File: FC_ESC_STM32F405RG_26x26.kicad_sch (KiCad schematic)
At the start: 233 parts, among them J1 MOTOR, J10 UART4, J12 Conn_02x02_Odd_Even, J13 ALARM, J14 LED_STRIP, J15 RC, J16 MOTOR, J17 MOTOR, J18 MOTOR, J19 MOTOR, J2 Conn_02x04_Odd_Even, J20 USB_A, J21 ESC_PROG, J22 MOTOR, J23 ESC_PROG, J24 ESC_PROG, J25 ESC_PROG, J26 MOTOR, J3 Debugger, J4 MOTOR, J5 RSSI, J6 I2C2_UART3, J7 SD CARD, J8 UART1, J9 UART6, Q1 SIZ200, Q10 SIZ200, Q11 SIZ200, Q12 SIZ200, Q2 SIZ200, Q3 SIZ200, Q4 SIZ200, Q5 SIZ200, Q6 SIZ200, Q7 SIZ200, Q8 SIZ200, Q9 SIZ200, U1 EFM8BB21, U10 FD6288Q, U11 outline, U12 MPU-6000, U13 BMP280, U15 STM32F405RGTx, U16 TPS54331D, U2 EFM8BB21, U3 TPS54560BDDA, U4 FD6288Q, U5 FD6288Q, U6 AT7456, U7 EFM8BB21, U8 EFM8BB21, U9 FD6288Q, Y1 8MHz, Y2 8Mhz

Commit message: update placement
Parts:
- removed J1, J22, J26, J4: MOTOR, Proj_footprint:MountingPad_1x3, symbol Connector_Generic:Conn_01x03
- removed J10: UART4, Proj_footprint:MoutingPad_1x4, symbol Connector_Generic:Conn_01x04
- removed J15: RC, Connector_PinHeader_2.54mm:PinHeader_1x03_P2.54mm_Vertical, symbol Connector_Generic:Conn_01x03
- removed J7: SD CARD, Proj_footprint:MountingPad_1x6, symbol Connector_Generic:Conn_01x06
- removed J9: UART6, Proj_footprint:MoutingPad_1x4, symbol Connector_Generic:Conn_01x04
- added J1, J7: Conn_01x02, Proj_footprint:MountingPad_5VOUT, symbol Connector_Generic:Conn_01x02
- added J10: Conn_01x01, Proj_footprint:MountingPad_1x1, symbol Connector_Generic:Conn_01x01
- added J11: Conn_01x02, Proj_footprint:MountingPad_1x2, symbol Connector_Generic:Conn_01x02
- added J4: Conn_01x04, Proj_footprint:MountingPad_1x4, symbol Connector_Generic:Conn_01x04
- added J9: LED_STRIP, Proj_footprint:MountingPad_1x3, symbol Connector_Generic:Conn_01x03
- J13, J14, J5: footprint Connector_PinHeader_2.54mm:PinHeader_1x03_P2.54mm_Vertical -> Proj_footprint:MountingPad_1x3
- J6: value I2C2_UART3 -> Conn_01x04; footprint Proj_footprint:MoutingPad_1x4 -> Proj_footprint:MountingPad_1x4
- J8: value UART1 -> Conn_01x04; footprint Proj_footprint:MoutingPad_1x4 -> Proj_footprint:MountingPad_1x4
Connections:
- net +5V: now also J1.2 (Pin_2), J7.2 (Pin_2), J9.1 (Pin_1)
- net 3V3_FC: no longer J6.1 (Pin_1), J8.1 (Pin_1)
- net GND: now also J1.1 (Pin_1), J7.1 (Pin_1), J9.3 (Pin_3); no longer J6.4 (Pin_4), J8.4 (Pin_4)
- net OSD_VIDEO_IN: now also J11.1 (Pin_1)
- net OSD_VIDEO_OUT: now also J11.2 (Pin_2)
- net RCIN_INT: now also J10.1 (Pin_1)
- net SENS_RSSI: now also J4.1 (Pin_1)
- net SPI2_CLK: now also J6.4 (Pin_4)
- net SPI2_CS: now also J6.1 (Pin_1)
- net SPI2_MISO: now also J6.3 (Pin_3)
- net SPI2_MOSI: now also J6.2 (Pin_2)
- net STM32_PB10: now also J4.3 (Pin_3); no longer J6.2 (Pin_2)
- net STM32_PB11: now also J4.4 (Pin_4); no longer J6.3 (Pin_3)
- net UART1_RX: now also J8.3 (Pin_3); no longer J8.2 (Pin_2)
- net UART1_TX: now also J8.4 (Pin_4); no longer J8.3 (Pin_3)
- net UART6_RX: now also J8.2 (Pin_2)
- net UART6_TX: now also J8.1 (Pin_1)
- net PWM5 renamed STM32_PA1
- net STM32_PA1: now also J4.2 (Pin_2)
- net PWM6: no longer names the net of U15.41 (PA8)
- net PWM7 renamed PWM_OUT
- net PWM_OUT: now also J9.2 (Pin_2)
- net PWM8: no longer names the net of U15.40 (PC9)
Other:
- moved on the sheet: J3

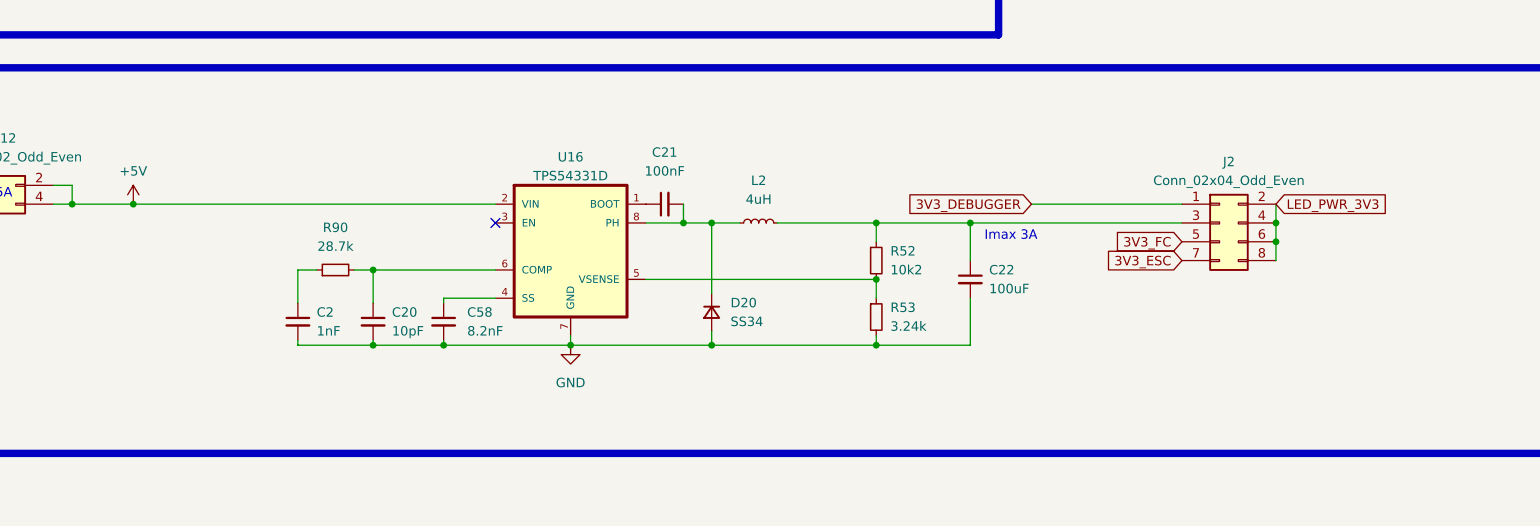
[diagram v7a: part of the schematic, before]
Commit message: update placement
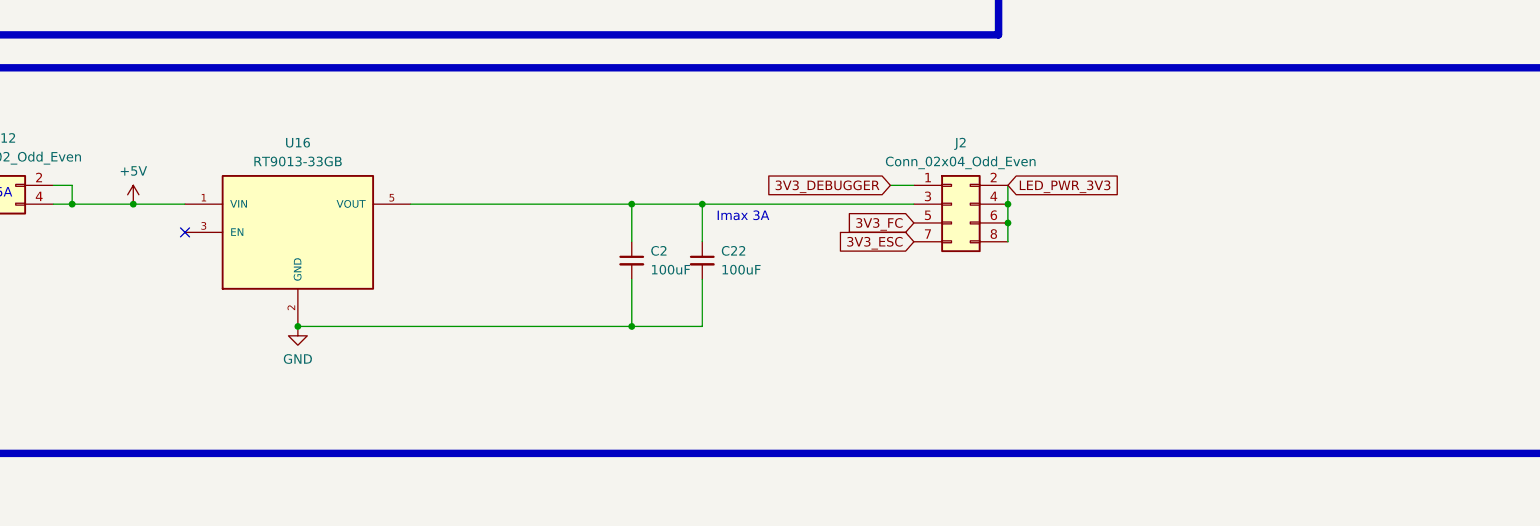
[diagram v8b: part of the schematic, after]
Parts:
- removed C20: 10pF, Capacitor_SMD:C_0402_1005Metric_Pad0.74x0.62mm_HandSolder, symbol Device:C_Small
- removed C21: 100nF, Capacitor_SMD:C_0402_1005Metric_Pad0.74x0.62mm_HandSolder, symbol Device:C_Small
- removed C58: 8.2nF, Capacitor_SMD:C_0402_1005Metric_Pad0.74x0.62mm_HandSolder, symbol Device:C_Small
- removed D20: SS34, Diode_SMD:D_SMA, symbol Device:D_Small
- removed L2: 4uH, Proj_footprint:Inductor, symbol Device:L_Small
- removed R52: 10k2, Resistor_SMD:R_0402_1005Metric_Pad0.72x0.64mm_HandSolder, symbol Device:R_Small
- removed R53: 3.24k, Resistor_SMD:R_0402_1005Metric_Pad0.72x0.64mm_HandSolder, symbol Device:R_Small
- removed R90: 28.7k, Resistor_SMD:R_0402_1005Metric_Pad0.72x0.64mm_HandSolder, symbol Device:R_Small
- removed U16: TPS54331D, Proj_footprint:SOIC-8-1EP_3.9x4.9mm_P1.27mm_EP2.29x3mm, symbol TPS54331:TPS54331D
- added U16: RT9013-33GB, Package_TO_SOT_SMD:SOT-23-5, symbol RT9013:RT9013-33GB
- C2: value 1nF -> 100uF; footprint Capacitor_SMD:C_0402_1005Metric_Pad0.74x0.62mm_HandSolder -> Capacitor_SMD:C_1210_3225Metric_Pad1.33x2.70mm_HandSolder
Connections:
- net +5V: now also U16.1 (VIN)
- net GND: now also U16.2 (GND)
- net at C22.1, J2.3 (Pin_3): now also C2.1, U16.5 (VOUT)
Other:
- moved on the sheet: C22, J2
